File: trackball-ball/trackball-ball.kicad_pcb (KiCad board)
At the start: 4 copper layers, 27.5 x 27.5 mm, 92 parts, among them J1 FH28D-28S, J2 JST-PH-3, J3 JST-PH-2, Q1 DMG6968U, U1 NRF52810-QCAA, U2 CY8CMBR3116-0x37, U3 CY8CMBR3116-0x38, U4 LTC4120-4.2, U5 BQ29700, U6 XC6206P302, Y1 32MHz-CL9pF

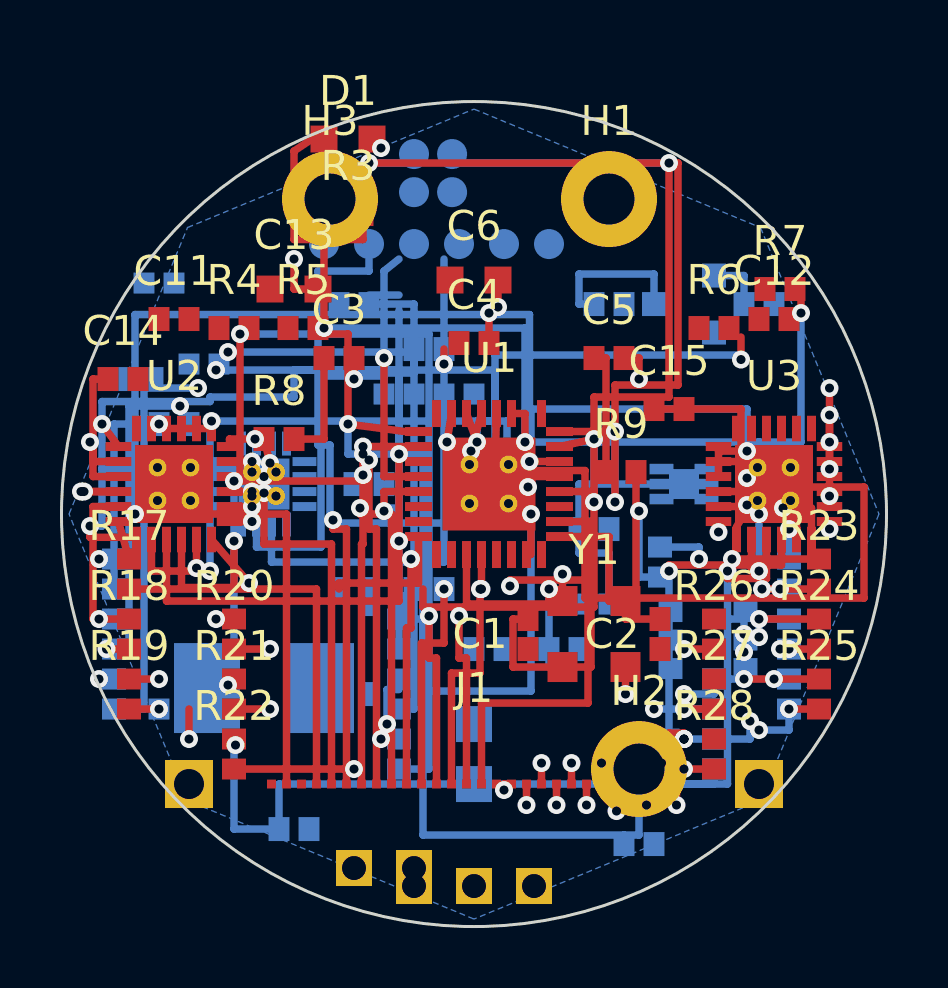
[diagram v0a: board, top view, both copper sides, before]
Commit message: ball: Q10a/Q13a/Q14d(ii)/Q15a owner verdicts + docs (driver-preserved WIP, 2026-10-10)
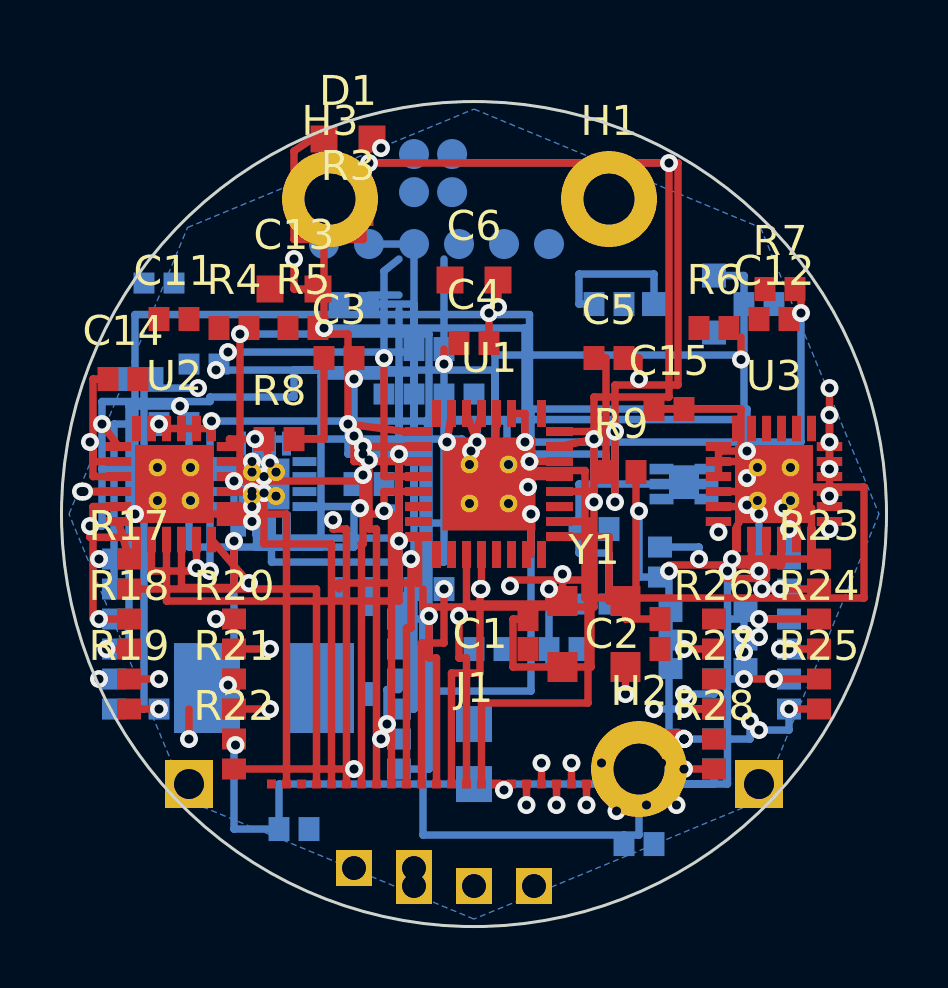
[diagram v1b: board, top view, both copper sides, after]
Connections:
- C18 pad 1: U4_INTVCC -> GND
- C18 pad 2: GND -> U4_INTVCC
- U1 pad 5: CHRG -> FAULT
- U1 pad 6: FAULT -> CHRG
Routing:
- net +3V0: track 9.65 -> 48.9 mm
- net U4_INTVCC: track 0.00 -> 11.8 mm
- net FAULT: track 17.1 -> 22.2 mm, vias 0 -> 1
- net TP_SPARE: track 19.2 -> 16.3 mm
- net CELL_N: track 0.00 -> 1.55 mm
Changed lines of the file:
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@@
     (pad "3" smd rect (at -2.35 0.75) (size 0.9 0.3) (layers "F.Cu" "F.Paste" "F.Mask") (pinfunction "") (pintype ""))
     (pad "4" smd rect (at -2.35 0.25) (size 0.9 0.3) (layers "F.Cu" "F.Paste" "F.Mask") (net 45 "VBAT_SNS") (pinfunction "") (pintype ""))
-    (pad "5" smd rect (at -2.35 -0.25) (size 0.9 0.3) (layers "F.Cu" "F.Paste" "F.Mask") (net 46 "CHRG") (pinfunction "") (pintype ""))
-    (pad "6" smd rect (at -2.35 -0.75) (size 0.9 0.3) (layers "F.Cu" "F.Paste" "F.Mask") (net 47 "FAULT") (pinfunction "") (pintype ""))
+    (pad "5" smd rect (at -2.35 -0.25) (size 0.9 0.3) (layers "F.Cu" "F.Paste" "F.Mask") (net 47 "FAULT") (pinfunction "") (pintype ""))
+    (pad "6" smd rect (at -2.35 -0.75) (size 0.9 0.3) (layers "F.Cu" "F.Paste" "F.Mask") (net 46 "CHRG") (pinfunction "") (pintype ""))
     (pad "7" smd rect (at -2.35 -1.25) (size 0.9 0.3) (layers "F.Cu" "F.Paste" "F.Mask") (net 32 "I2C_SDA") (pinfunction "") (pintype ""))
     (pad "8" smd rect (at -2.35 -1.75) (size 0.9 0.3) (layers "F.Cu" "F.Paste" "F.Mask") (net 33 "I2C_SCL") (pinfunction "") (pintype ""))
@@
     (property "Reference" "C18" (at 0 -1.6 0) (layer "B.SilkS") (effects (font (size 1 1) (thickness 0.15))))
     (property "Value" "2.2uF-X7R-0603-10V" (at 0 1.6 0) (layer "B.Fab") (effects (font (size 1 1) (thickness 0.15))))
-    (pad "1" smd rect (at -0.5 0) (size 0.7 0.8) (layers "B.Cu" "B.Paste" "B.Mask") (net 78 "U4_INTVCC") (pinfunction "") (pintype ""))
-    (pad "2" smd rect (at 0.5 0) (size 0.7 0.8) (layers "B.Cu" "B.Paste" "B.Mask") (net 1 "GND") (pinfunction "") (pintype ""))
+    (pad "1" smd rect (at -0.5 0) (size 0.7 0.8) (layers "B.Cu" "B.Paste" "B.Mask") (net 1 "GND") (pinfunction "") (pintype ""))
+    (pad "2" smd rect (at 0.5 0) (size 0.7 0.8) (layers "B.Cu" "B.Paste" "B.Mask") (net 78 "U4_INTVCC") (pinfunction "") (pintype ""))
     (fp_rect (start -1.05 -0.65) (end 1.05 0.65) (stroke (width 0.05) (type solid)) (layer "B.CrtYd") (fill none))
   )
@@
   (via (at 96.5 88.3) (size 0.6) (drill 0.3) (layers "F.Cu" "B.Cu") (net 42 "SWDIO"))
   (segment (start 96.5 88.3) (end 98 88.3) (width 0.25) (layer "B.Cu") (net 42 "SWDIO"))
-  (segment (start 94.8 91.9) (end 94.8 97.7) (width 0.25) (layer "B.Cu") (net 39 "TP_SPARE"))
-  (segment (start 95.2 100.3) (end 101.9 100.3) (width 0.25) (layer "B.Cu") (net 39 "TP_SPARE"))
-  (segment (start 94.8 97.7) (end 95.2 97.7) (width 0.25) (layer "B.Cu") (net 39 "TP_SPARE"))
-  (segment (start 95.2 97.7) (end 95.2 100.3) (width 0.25) (layer "B.Cu") (net 39 "TP_SPARE"))
+  (segment (start 98 100.3) (end 101.9 100.3) (width 0.25) (layer "B.Cu") (net 39 "TP_SPARE"))
+  (segment (start 96.5 91) (end 98 91) (width 0.25) (layer "B.Cu") (net 39 "TP_SPARE"))
+  (segment (start 98 91) (end 98 100.3) (width 0.25) (layer "B.Cu") (net 39 "TP_SPARE"))
   (segment (start 101.9 100.3) (end 101.9 100) (width 0.25) (layer "B.Cu") (net 39 "TP_SPARE"))
   (via (at 101.9 100) (size 0.6) (drill 0.3) (layers "F.Cu" "B.Cu") (net 39 "TP_SPARE"))
   (segment (start 101.9 100) (end 101.9 101.35) (width 0.25) (layer "F.Cu") (net 39 "TP_SPARE"))
-  (segment (start 94.8 91.9) (end 96.5 91.9) (width 0.25) (layer "B.Cu") (net 39 "TP_SPARE"))
-  (segment (start 96.5 91.9) (end 96.5 91.5) (width 0.25) (layer "B.Cu") (net 39 "TP_SPARE"))
   (segment (start 98.15 100.75) (end 98.15 102.3) (width 0.25) (layer "F.Cu") (net 48 "U1_DEC1"))
   (segment (start 98.15 102.3) (end 95.5 102.3) (width 0.25) (layer "F.Cu") (net 48 "U1_DEC1"))
@@
   (segment (start 97 91.9) (end 97.5 91.5) (width 0.25) (layer "B.Cu") (net 46 "CHRG"))
   (segment (start 97 95.4) (end 97 94.8) (width 0.25) (layer "B.Cu") (net 46 "CHRG"))
-  (via (at 97 94.8) (size 0.6) (drill 0.3) (layers "F.Cu" "B.Cu") (net 46 "CHRG"))
-  (segment (start 97 94.8) (end 97 98.75) (width 0.25) (layer "F.Cu") (net 46 "CHRG"))
-  (segment (start 97 98.75) (end 98.15 98.75) (width 0.25) (layer "F.Cu") (net 46 "CHRG"))
+  (via (at 97 94.8) (size 0.6) (drill 0.3) (layers "F.Cu" "B.Cu") (net 47 "FAULT"))
+  (segment (start 97 94.8) (end 97 98.75) (width 0.25) (layer "F.Cu") (net 47 "FAULT"))
+  (segment (start 97 98.75) (end 98.15 98.75) (width 0.25) (layer "F.Cu") (net 47 "FAULT"))
+  (segment (start 96 95.4) (end 96 97.4) (width 0.25) (layer "B.Cu") (net 46 "CHRG"))
+  (via (at 96 97.4) (size 0.6) (drill 0.3) (layers "F.Cu" "B.Cu") (net 46 "CHRG"))
+  (segment (start 96 97.4) (end 96 98.25) (width 0.25) (layer "F.Cu") (net 46 "CHRG"))
+  (segment (start 96 98.25) (end 98.15 98.25) (width 0.25) (layer "F.Cu") (net 46 "CHRG"))
+  (segment (start 94.75 99.75) (end 96 99.75) (width 0.25) (layer "B.Cu") (net 78 "U4_INTVCC"))
+  (segment (start 96 99.75) (end 96 101.1) (width 0.25) (layer "B.Cu") (net 78 "U4_INTVCC"))
+  (segment (start 96 101.1) (end 90.5 101.1) (width 0.25) (layer "B.Cu") (net 78 "U4_INTVCC"))
+  (segment (start 90.5 101.1) (end 90.5 97.4) (width 0.25) (layer "B.Cu") (net 78 "U4_INTVCC"))
   (segment (start 93.25 100.35) (end 93.25 101.6) (width 0.25) (layer "B.Cu") (net 47 "FAULT"))
   (segment (start 93.25 101.6) (end 99 101.6) (width 0.25) (layer "B.Cu") (net 47 "FAULT"))
@@
   (segment (start 108 92.05) (end 109 92.05) (width 0.25) (layer "B.Cu") (net 3 "+3V0"))
   (segment (start 109 92.05) (end 109 93) (width 0.25) (layer "B.Cu") (net 3 "+3V0"))
+  (segment (start 109 93) (end 109 96.85) (width 0.25) (layer "B.Cu") (net 3 "+3V0"))
+  (segment (start 109 96.85) (end 98.45 96.85) (width 0.25) (layer "B.Cu") (net 3 "+3V0"))
+  (segment (start 98.45 96.85) (end 98.45 100.8) (width 0.25) (layer "B.Cu") (net 3 "+3V0"))
+  (segment (start 98.45 100.8) (end 93 100.8) (width 0.25) (layer "B.Cu") (net 3 "+3V0"))
+  (segment (start 93 100.8) (end 93 97.5) (width 0.25) (layer "B.Cu") (net 3 "+3V0"))
+  (segment (start 93 97.5) (end 99.6 97.5) (width 0.25) (layer "B.Cu") (net 3 "+3V0"))
+  (segment (start 99.6 97.5) (end 99.6 98) (width 0.25) (layer "B.Cu") (net 3 "+3V0"))
+  (segment (start 99.6 98) (end 104.4 98) (width 0.25) (layer "B.Cu") (net 3 "+3V0"))
+  (segment (start 104.4 98) (end 104.4 98.2) (width 0.25) (layer "B.Cu") (net 3 "+3V0"))
+  (segment (start 106.25 98.5) (end 107.8 98.5) (width 0.25) (layer "B.Cu") (net 5 "CELL_N"))
   (segment (start 96 94.8) (end 96 95.5) (width 0.25) (layer "F.Cu") (net 1 "GND"))
   (via (at 96 95.5) (size 0.6) (drill 0.3) (layers "F.Cu" "B.Cu") (net 1 "GND"))

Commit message: ball: driver-preserved WIP (2026-10-11 recovery, ANT cascade owner-pending)
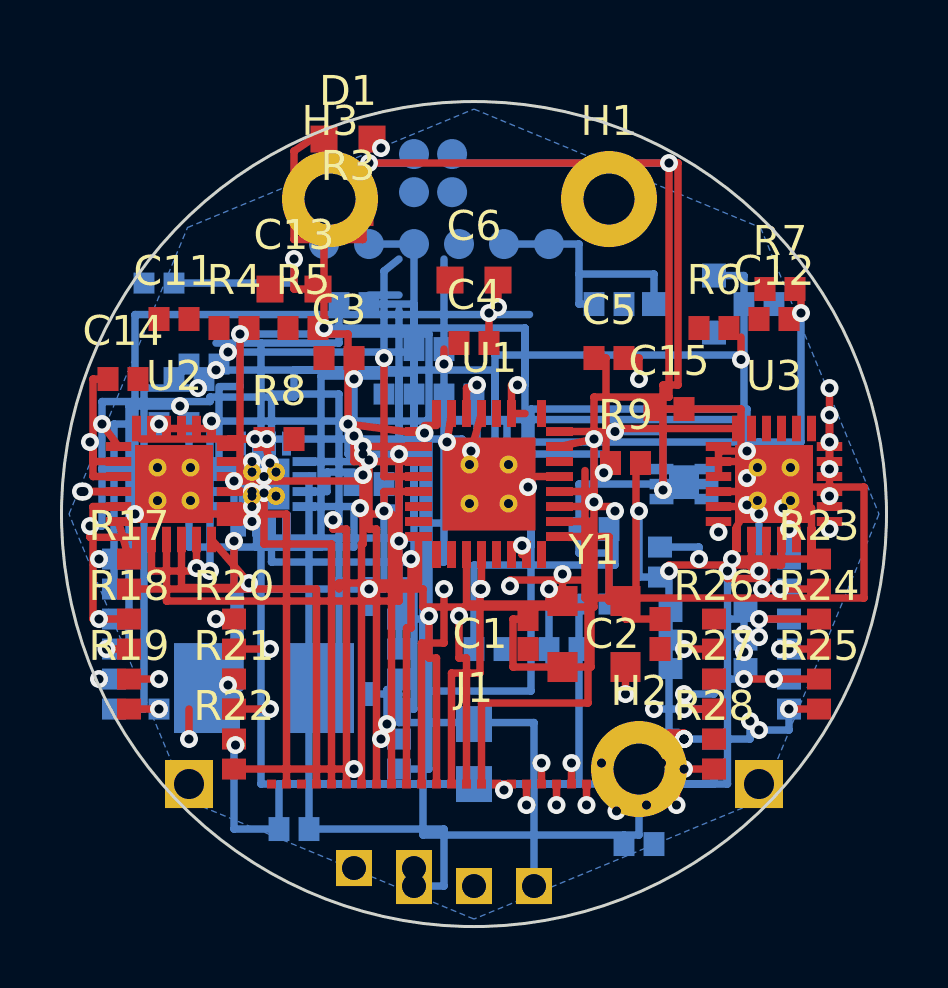
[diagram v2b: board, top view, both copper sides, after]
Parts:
- moved C20 1.70 mm to (90.5, 95.5)
- moved C8 1.50 mm to (97.0, 102.5)
- moved R9 0.34 mm to (105.0, 98.3)
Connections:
- C10 pad 1: U3_DEC2 -> U1_DEC4
- C9 pad 1: U3_DEC4 -> U1_DEC3
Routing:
- net VBAT: track 5.00 -> 49.4 mm
- net VIN_RX: track 0.00 -> 18.6 mm
- net SW_RX: track 0.00 -> 14.2 mm
- net DHC_U4: track 0.00 -> 13.7 mm
- net DHC_SNS: track 0.00 -> 11.6 mm
- net U1_DEC3: track 0.00 -> 11.4 mm, vias 0 -> 1
- net +3V0: track 48.9 -> 54.8 mm, vias 0 -> 3
- net ANT_FEED: track 39.8 -> 33.8 mm, vias 2 -> 1
- net XRES2: track 32.7 -> 27.8 mm
- net GND: track 15.4 -> 19.5 mm
- net LED_DOT: track 15.5 -> 17.4 mm
- net U4_BOOST: track 0.00 -> 1.90 mm
- net U1_DEC2: track 11.3 -> 13.1 mm, vias 0 -> 1
- net HI2: track 23.1 -> 24.0 mm
- net SWDCLK: track 25.1 -> 24.3 mm

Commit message: ball: driver gate-5 DRC run — pcb syntax repairs + 1759-violation report (WIP, NOT clean)
Syntax repairs (mechanical, no geometry/electrical intent change) so the
board parses under KiCad 10.0.6 (kicad-cli/pcbnew both refused to load it):
- zone (fill ...) gained required leading yes token (3 zones)
- zone (connect_pads ...) reduced to (clearance X) per v10 grammar (3 zones)
- keepout tokens yes/no -> not_allowed/allowed (antenna keepout zone)
- (net N "name") -> (net N) on 720 tracks/vias (v10 parser rejects the
  name token; net numbers untouched; footprint pads keep the two-token
  form, which v10 still parses)

Gate-5 DRC (kicad-cli pcb drc, trackball-ball.kicad_dru applied):
1759 violations / 89 unconnected — NOT clean. Breakdown: 499 clearance,
199 shorting_items, 199 hole_clearance, 199 solder_mask_bridge,
126 silk_over_copper, 106 nonmirrored_text_on_back_layer, 101 tracks_crossing,
89 unconnected_items, 79 courtyards_overlap, 73 lib_footprint_mismatch
(warnings), 57 hole_to_hole, 33 silk_overlap, 29 copper_edge_clearance,
14 items_not_allowed, 13 track_width, 13 silk_edge_clearance, 10 track_dangling,
5 lib_footprint_issues, 2 via_dangling, 1 length_out_of_range
(ant_feed_length 46.78mm vs 20mm max — real RF-rule finding),
1 holes_co_located. Full report: trackball-ball-drc.rpt (this commit).

ERC: kicad-cli sch erc fails to LOAD the schematic (parse-level) — TBD.

Next: agent triages the report (real vs artifact), fixes, re-runs DRC.
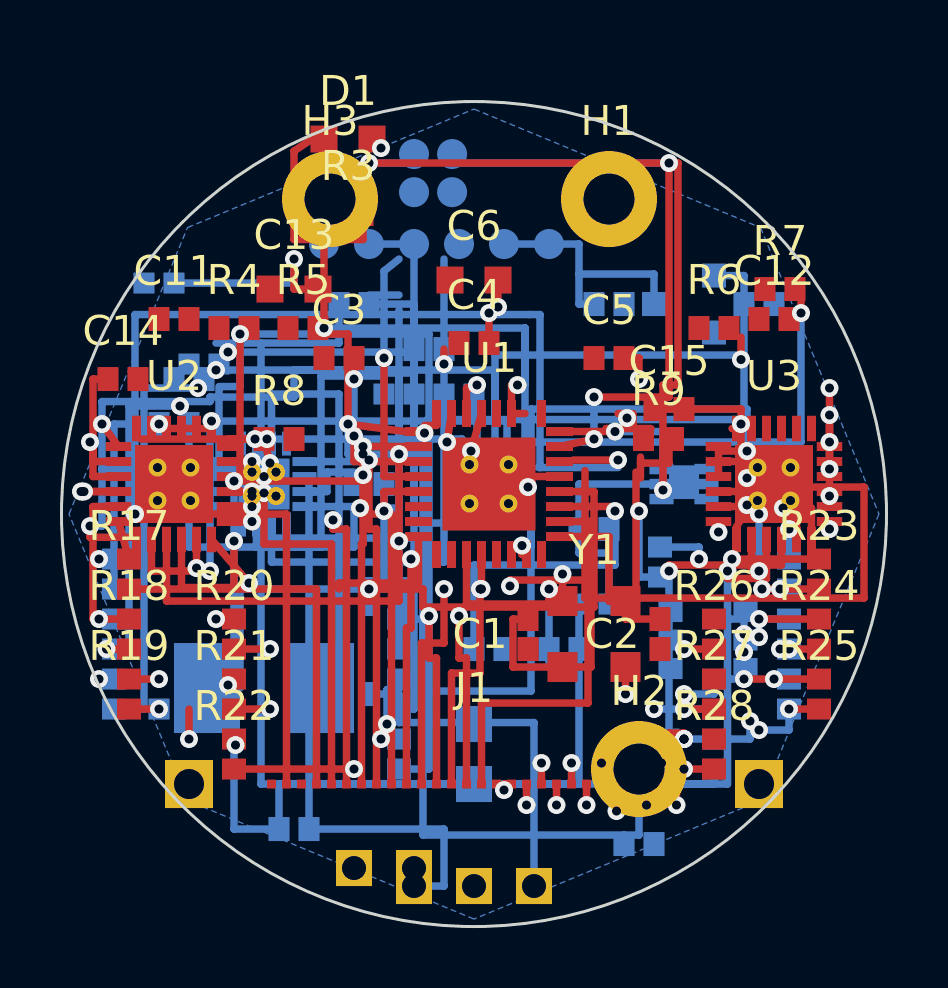
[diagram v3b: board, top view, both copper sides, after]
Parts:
- moved R9 1.36 mm to (106.2, 97.5)
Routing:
- net +3V0: track 54.8 -> 44.3 mm, vias 3 -> 4
- net ANT_FEED: track 33.8 -> 43.5 mm, vias 1 -> 2
- net SWDIO: track 28.6 -> 24.4 mm
- net XRES2: track 27.8 -> 30.1 mm

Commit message: ball: driver gate-6 DRC run — VBAT<->SDA + ...815/SDA short repairs verified, 1736 violations / 87 unconnected / 92 parity (WIP, NOT clean)
Tool-run (kicad-cli 10.0.6, pcb drc --schematic-parity + sch erc --severity-all, snapshot 2026-10-13 15:45 CDT):
- DRC: 1736 violations / 87 unconnected items / 92 schematic parity issues
- Both target shorts from the VBAT-south-move cluster are GONE from shorting_items:
  (m) VBAT<->SDA 10mm overlap on B.Cu y109 and (o) ...815/SDA touch — no VBAT<->I2C_SDA pair remains in the report
- ERC: report saved alongside (build/trackball-ball-erc-20261013-1545.json)
- Remaining shorting_items still ~199 (east-field census continues); most unconnected items are the known GND-pour rats pending the F.Cu pour (Q-F, parked)
Reports: build/trackball-ball-drc-20261013-1545.json, build/trackball-ball-erc-20261013-1545.json
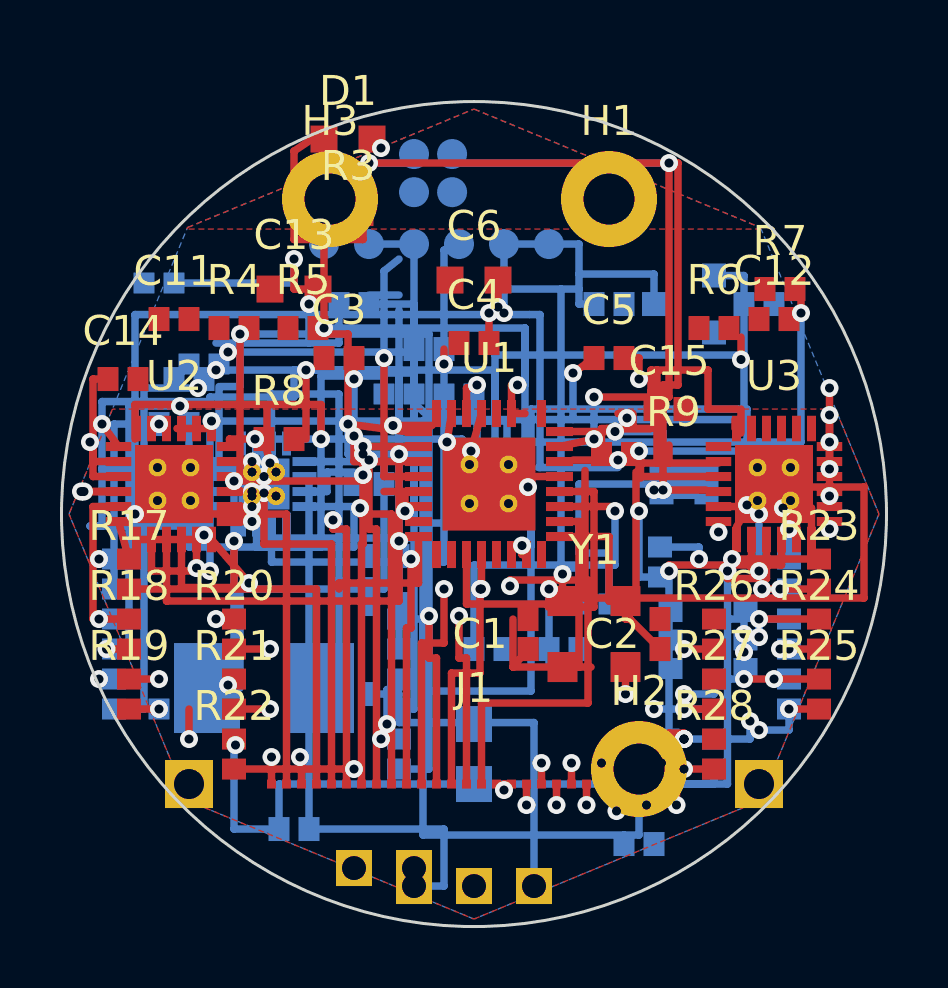
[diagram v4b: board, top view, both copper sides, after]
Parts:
- moved C23 3.54 mm to (100.6, 99.5)
- moved R9 1.49 mm to (104.8, 98.0)
- moved C8 1.10 mm to (97.0, 101.4)
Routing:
- net +3V0: track 44.3 -> 56.7 mm
- net VBAT: track 49.4 -> 42.0 mm, vias 0 -> 2
- net U1_DEC2: track 13.1 -> 6.53 mm, vias 1 -> 0
- net XRES1: track 32.0 -> 38.3 mm, vias 3 -> 4
- net U3_CMOD: track 5.40 -> 11.0 mm
- net U3_CS3: track 26.6 -> 31.5 mm
- net U3_CS2: track 30.4 -> 32.1 mm
- net U3_CS5: track 34.3 -> 35.4 mm
- net GND: track 19.5 -> 20.5 mm, vias 15 -> 17
- net FAULT: track 22.2 -> 22.7 mm
- added copper zone on F.Cu, net GND
